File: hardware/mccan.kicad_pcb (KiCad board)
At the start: 8 copper layers, 200 x 140 mm, 238 parts, among them J1 PWR pigtail -> SS1.5 3w, J2 Prog/UART, J3 FL pigtail -> SS1.0 key A / b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, J4 FR pigtail -> SS1.0 key B / g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, J5 RL pigtail -> SS1.0 key C / b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, J6 RR pigtail -> SS1.0 key D / n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, J7 DENALI pigtail -> SS1.5 3w, J8 CAN pigtail -> SS1.0 2w, Q10 IPT008N06NM5LF, Q11 IPT008N06NM5LF, Q12 MMBT3904, Q2 MMBT3904, Q3 MMBT3904, Q4 NX5020UNBKS, Q5 NX5020UNBKS, Q6 NX5020UNBKS, Q7 NX5020UNBKS, Q8 NX5020UNBKS, Q9 NX5020UNBKS, SW1 BOOT, SW2 EN/RESET, U1 LM5164DDA, U10 LTC4380HMS-2, U2 LM5164DDA, U3 LM51571-Q1, U4 DML3017LDC, U5 ESP32-WROOM-32E-N8, U6 TJA1042T/3, U7 PCA9685PW/Q900, U8 ADG706, U9 BTS7008-2EPA

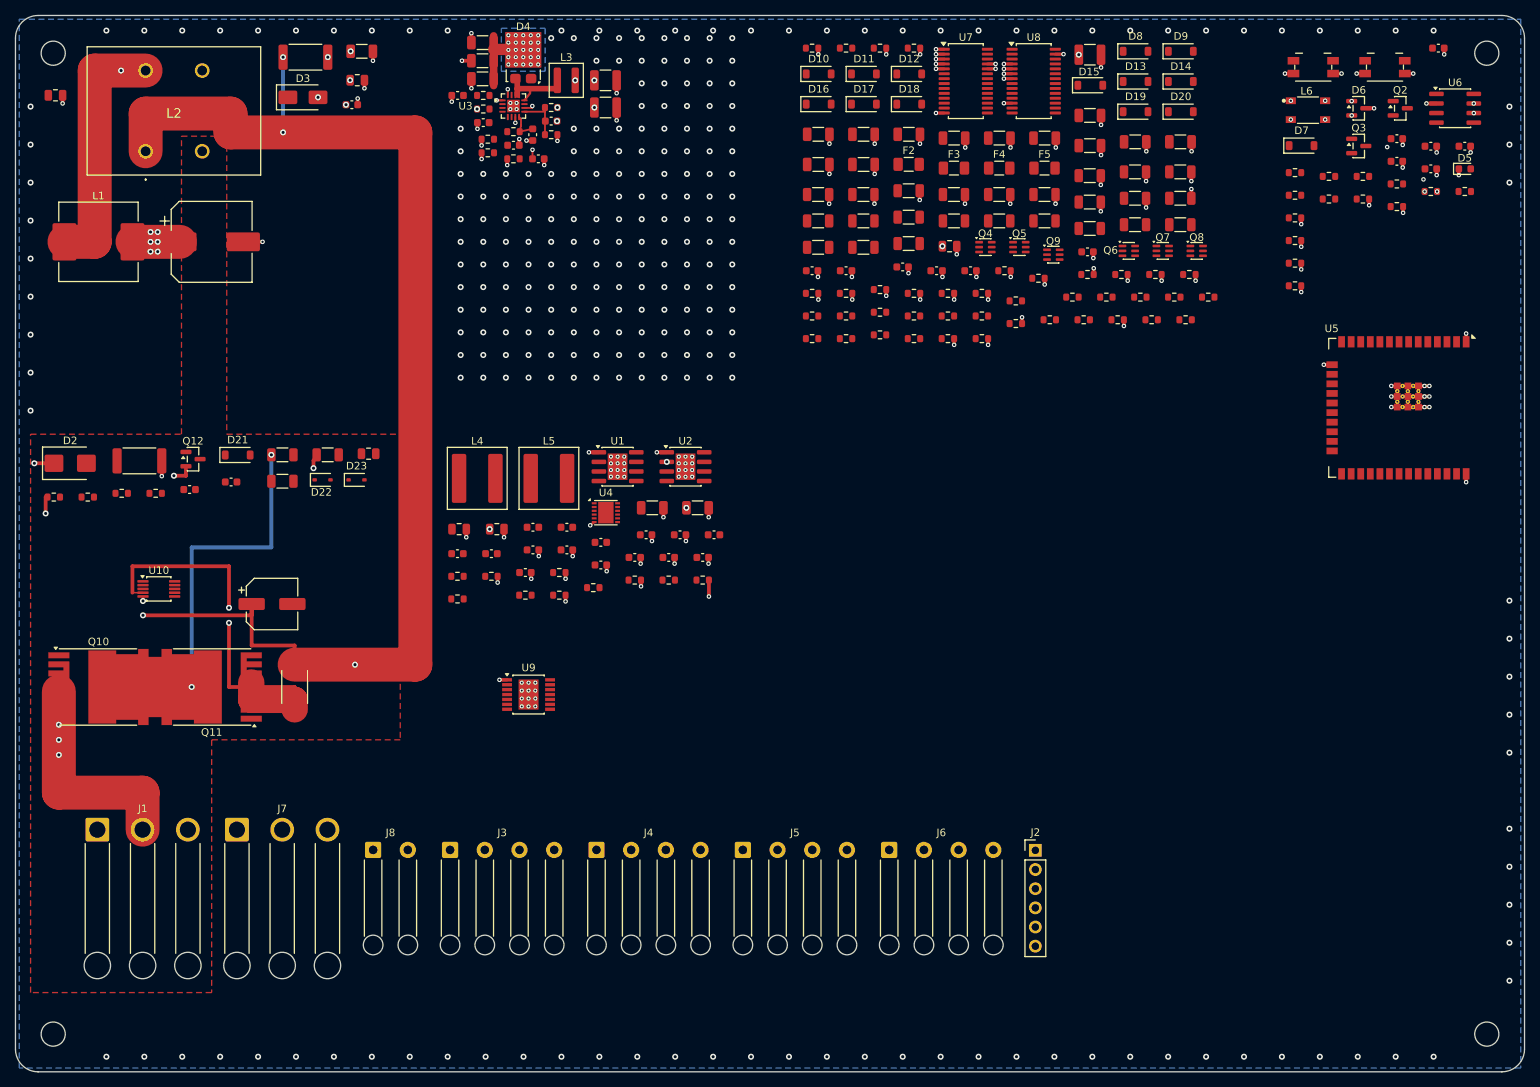
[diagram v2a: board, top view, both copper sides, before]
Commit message: hw(pcb): the router's copper, on four layers with room to use them
122 of 139 signal nets, against 122 on the six-layer board. Graded by
check_geometry.py before a single segment was admitted -- the tool will go below the
sizes you give it and exit 0, so its own graders being content means nothing.

KiCadRoutingTools closed 17-net worth of the internal router's channel starvation on
the first pass; freeze_routes.py dropped 2 sub-10um nubs (5um each, well under the
0.01mm floor) that check_geometry.py correctly refused to admit raw. No copper the
repo decided by hand was lost -- freeze_routes.py's additive diff confirmed it.

DRC: 0 errors, 0 schematic parity, 19 unconnected (18 distinct nets: 17 signal nets
the router could not close plus one pre-existing GND drop gap at U4.4 from an earlier
task, unrelated to this run). Dramatically down from the six-layer board's 72, and
under the 21-net router-attributable bar on the first router pass, before any Step 6
hand-closing. Left unclosed rather than reached for --rip-existing-nets: routing-tool.md
5.3 already tried that exact lever on this exact shortfall and it made things worse
(72 to 82 unconnected), because a rip is only a gain if the re-route succeeds and
granting authority just moves which nets lose.

Co-Authored-By: Claude Sonnet 5 <noreply@anthropic.com>
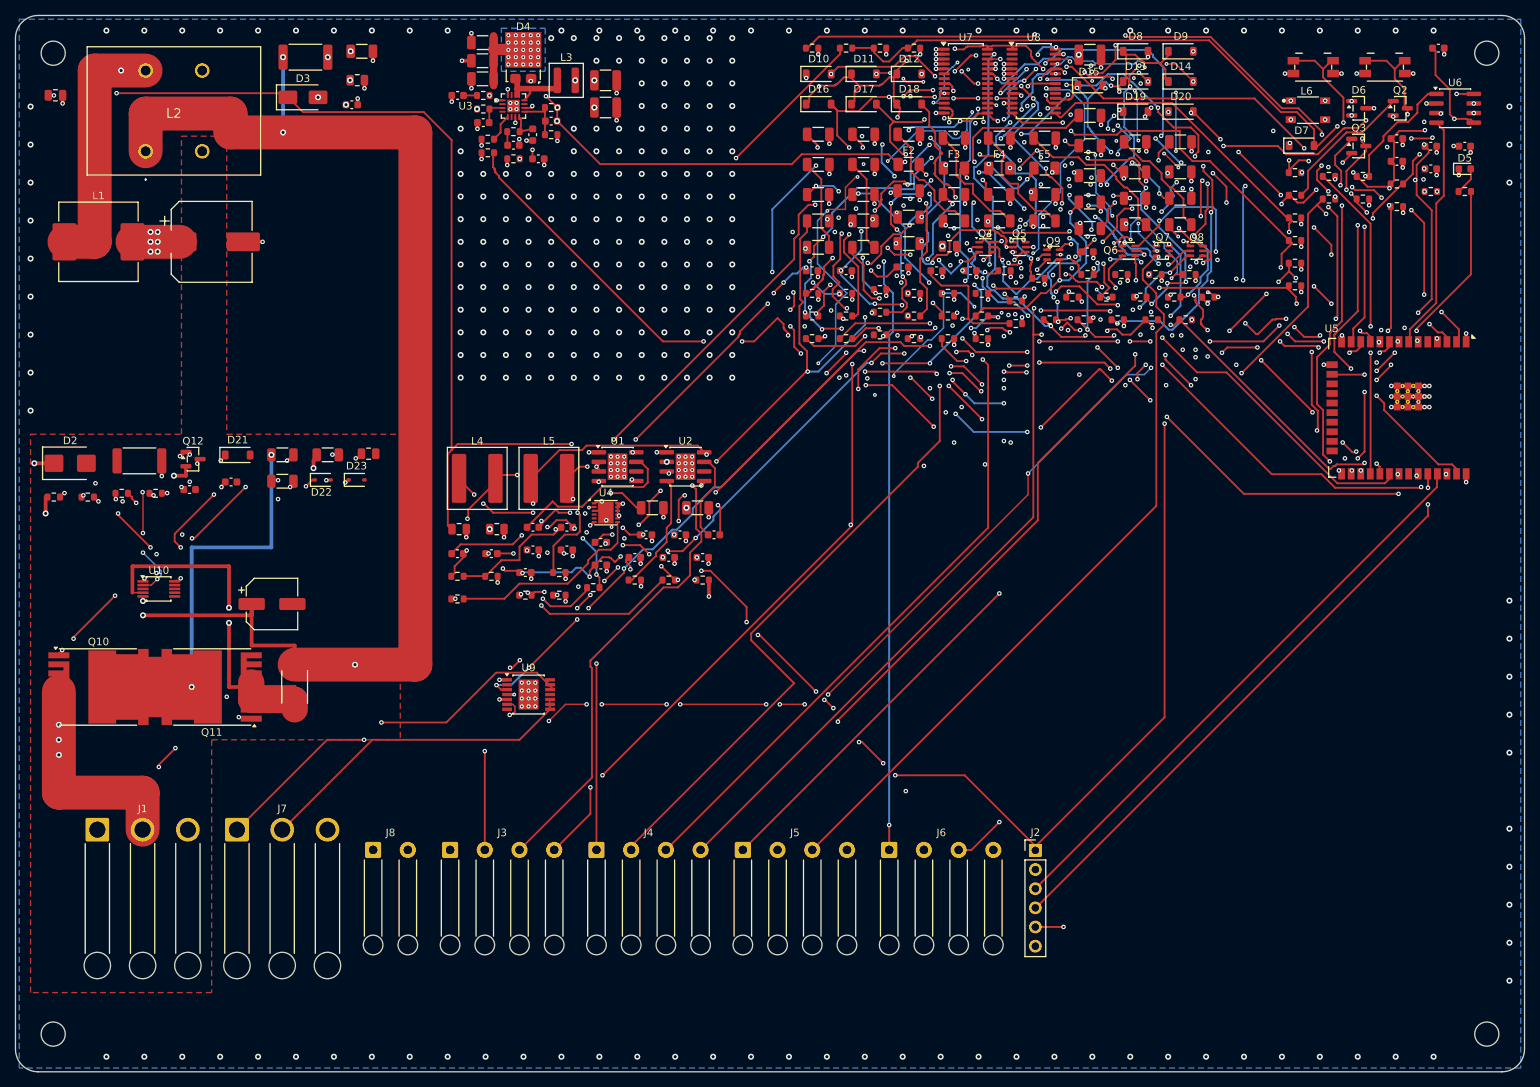
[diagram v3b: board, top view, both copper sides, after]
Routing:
- net /+3V3_ALW: track 0.00 -> 324.8 mm, vias 0 -> 38
- net /+3V3_SW: track 0.00 -> 267.3 mm, vias 0 -> 34
- net /+5V: track 0.00 -> 199.3 mm, vias 0 -> 18
- net /outputs/RET_FR_G: track 0.00 -> 176.6 mm, vias 0 -> 10
- net /outputs/RET_FL_B: track 0.00 -> 170.3 mm, vias 0 -> 12
- net /ISNS_DEN: track 0.00 -> 165.7 mm, vias 0 -> 23
- net /EN_BOOST: track 0.00 -> 155.2 mm, vias 0 -> 17
- net /outputs/RET_RR_G: track 0.00 -> 150.8 mm, vias 0 -> 12
- net /outputs/SENSE_FR_R: track 0.00 -> 150.7 mm, vias 0 -> 18
- net /IGN_IN: track 0.00 -> 144.4 mm, vias 0 -> 4
- net /RGB_ISNS: track 0.00 -> 142.4 mm, vias 0 -> 23
- net /VLOGIC_IN: track 0.00 -> 141.4 mm, vias 0 -> 5
- net /EN_3V3SW: track 0.00 -> 139.4 mm, vias 0 -> 22
- net /outputs/RET_RR_R: track 0.00 -> 139.2 mm, vias 0 -> 7
- net /outputs/PWM_RL_R: track 0.00 -> 137.3 mm, vias 0 -> 11
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
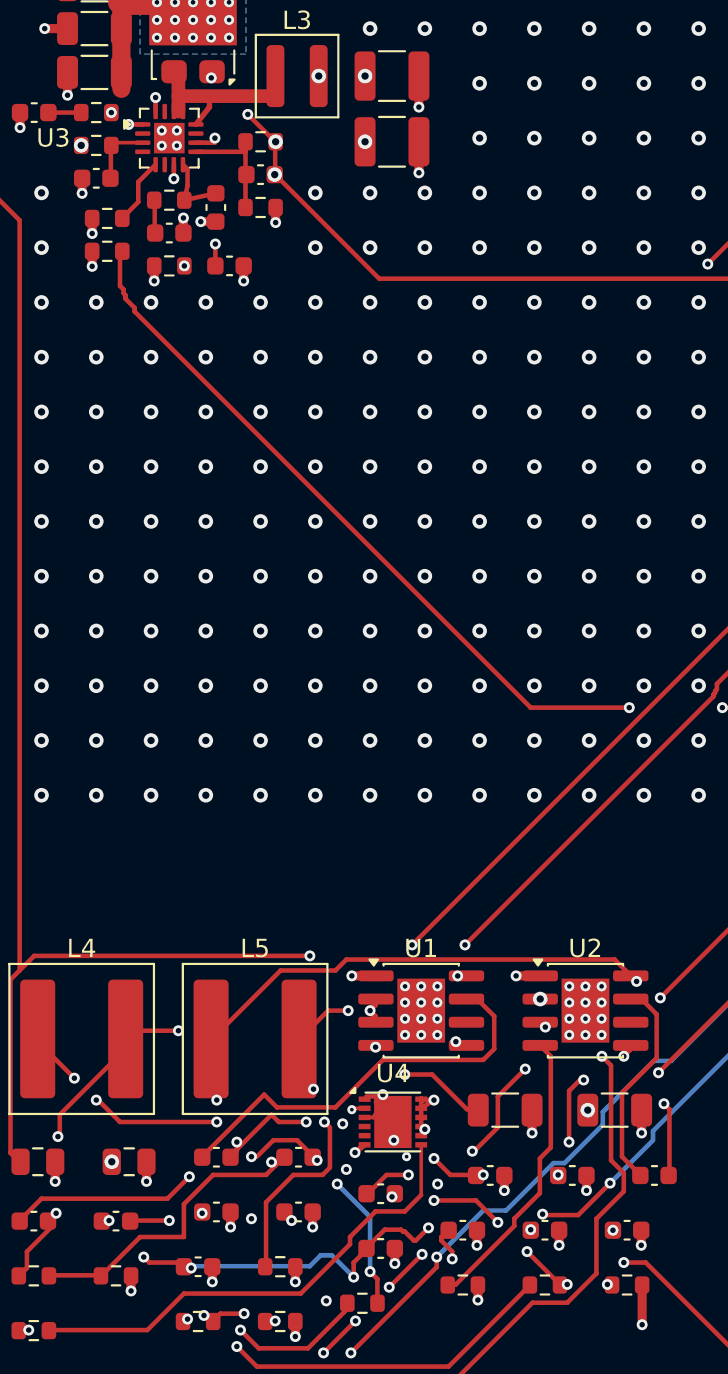
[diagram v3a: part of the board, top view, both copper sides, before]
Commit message: hw(pcb): close five of the seventeen open nets by hand
Net-(U3-MODE), Net-(U3-VCC), Net-(U4-SR), /EN_BOOST and the ground at U4
pin 6.  Four of the five were sealed into pockets by copper that is ours
to move, so three pieces move:

  - Net-(U3-SS)'s duck-under via goes 0.100 mm east.  The gate between
    U3 pin 12's pad corner and that via measured 0.884 mm where a 0.20 mm
    centreline needs 0.900; east makes it 0.957 and pin 11 (MODE) can
    leave its pad.
  - Net-(U3-VCC) claims U3 pin 1's ground drop site.  gnd_drops runs
    after ROUTES and re-places it, which the run confirms.
  - U4 pin 6's ground becomes a hand dogleg out of the pocket entirely.
    All 67 of its legal straight-stub sites lie in the same 1 mm box that
    pin 5 (SR) must via into; with any of them taken, flooding pin 5's
    F.Cu pocket gives 350 cells and zero legal via sites at every via
    size down to the board minimum.  With the dogleg, 8526 cells and 306
    sites, so both pins get served.

Every leg is measured against gen_pcb's own gap functions and the worst
slack of each net is in its comment: MODE +0.018, VCC +0.075, the U4 pin 6
dogleg +0.015, SR +0.025, /EN_BOOST +0.002 mm.

Also corrects gnd_drops' hand-snapshot comment, which claimed ROUTES
drew a dogleg for U4 pad 4.  It does not and cannot: pad 4 has zero legal
drop sites within 2.5 mm whether or not SR is drawn, so it stays on the
WARN line.  The pad that forced the mechanism is 6, not 4.

Unconnected pads 19 -> 15 (four ratsnest edges closed; U4 pin 6's ground
is now real copper but pad 4's edge stays open, which is Step 6's gap 14
and predates this work).  DRC 0 violations; courtyards, density,
geometry, vias, grounds, zone islands and plane width all pass.

Co-Authored-By: Claude Opus 5 <noreply@anthropic.com>
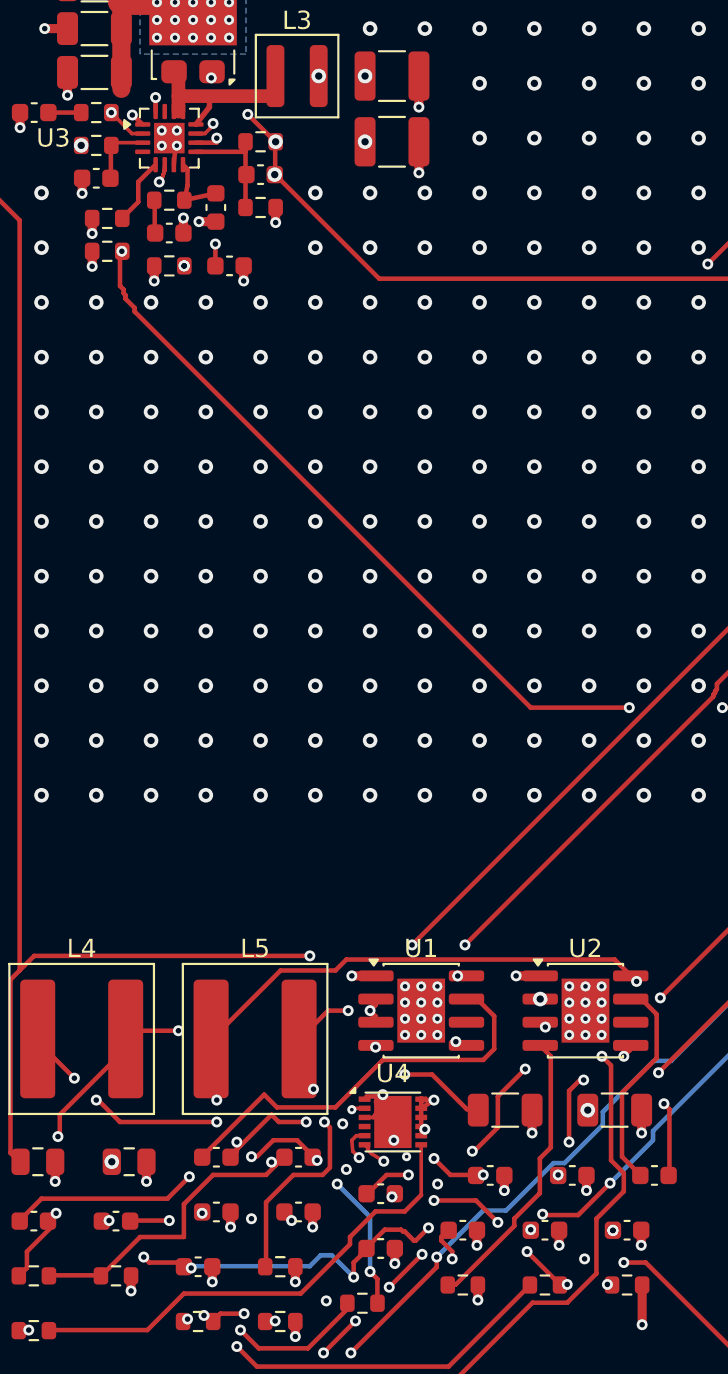
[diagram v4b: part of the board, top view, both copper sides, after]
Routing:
- net Net-(U4-SR): track 0.00 -> 18.9 mm, vias 1 -> 4
- net Net-(U3-MODE): track 0.00 -> 9.95 mm, vias 1 -> 3
- net /EN_BOOST: track 155.2 -> 160.6 mm, vias 17 -> 19
- net Net-(U3-VCC): track 0.00 -> 2.20 mm
- net GND: track 150.2 -> 152.1 mm, vias 435 -> 434

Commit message: hw(pcb): close U10_GATE and PWM_FL_R by hand
Two more of the thirteen open nets, unconnected pads 15 -> 13.

/power_input/U10_GATE, U10 pin 3 to R103 pad 1: F.Cu -> In5.Cu -> F.Cu,
14.5 mm, two 0.6/0.3 vias, worst slack +0.041 mm on the 0.200 mm Default
clearance.  The polyline starts 0.300 mm east of pin 3's pad centre -- still
inside the pad, which spans x 36.15..37.65 -- because a leg from the centre
itself meets the end cap of the /power_input/SNS run at (36.900, 96.500) at
exactly 0.200 mm.  Zero slack, measured.

/outputs/PWM_FL_R, U7 pin 6 to Q4 pad 2: F.Cu -> B.Cu -> F.Cu -> B.Cu ->
F.Cu, 53.8 mm and four vias for a 23 mm gap, worst slack +0.021 mm.  The
detour is not a preference.  U7's row is 0.65 mm pitch with 0.400 mm pads,
so adjacent pad edges are 0.25 mm apart and a 0.20 mm track needs 0.60 mm;
every escape is off a pad end.  Flooding pin 6's escape at 0.20 mm width
over x 140..158, y 24..54 reaches y = 39.05 on F.Cu and 34.55/34.45/34.35 on
In2/In5/B.Cu -- the MOSFET row at y = 50.7 is not in the set on any layer.
That box holds 2401 legal 0.60 mm via sites out of 216961.  So the route
goes west under the MCU to x = 132, ducks to F.Cu for the 4 mm at y 42..46
where B.Cu is full, then south-east and east along the y = 56 lane to Q4.

No existing copper moved.  Both ground drops that an earlier version of the
west haul displaced are back where the router left them, and that is worth
recording: gnd_drops.via_ok models a drop as the SQUARE enclosing it, while
routes() models the same via as the disc it is (the Step 6.0 ruling).  The
first version of the haul sat 0.225/0.231/0.238 mm from the drops at
(142.000, 32.925) and (133.875, 37.000) -- legal discs, gen_pcb rc=0 -- but
0.145 and 0.135/0.115 mm from their squares, so gnd_drops could not keep
either site and re-picked them at (144.175, 32.925) and (133.875, 37.200).
Those two land on the router's frozen copper, which gnd_drops cannot see
because it tests only TRACK_LOG: KiCad reported eight shorting_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
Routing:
- net /outputs/PWM_FL_R: track 8.26 -> 62.0 mm, vias 2 -> 6
- net /power_input/U10_GATE: track 27.0 -> 41.5 mm, vias 4 -> 6
